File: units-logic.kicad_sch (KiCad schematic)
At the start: 19 parts, among them U29 74AUC2G04, U30 74AUC2G32, U31 74AUC2G32, U34 74AUC2G32, U35 74AUC2G32, U37 74AUC2G08, U38 74AUC2G32, U40 74AUC2G32, U6 74AUC2G04, U7 74AUC2G04, U8 74AUC2G04

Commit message: add : alimentation
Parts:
- removed unit 2 of U10
- removed unit 3 of U30
- removed unit 3 of U31
- removed unit 3 of U34
- removed unit 3 of U35
- removed unit 3 of U7
- added C22, C23, C24, C25, C26, C27, C28, C29, C30, C31, C32, C33, C34, C35, C36: 0.1u, symbol Device:C
- added U28: (no value), Package_TO_SOT_SMD:SOT-23-6, symbol CornetPrisme_Library:SN74LVC1G11
- added unit 3 of U29
- added U42, U46, U47, U48: 74AUC2G32, symbol 74xGxx:74AUC2G32
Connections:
- net +1V8: now reaches U9.14 (VCC)
- net +1V8: now also U11.5 (VCC), U36.14 (VCC), U37.8 (VCC), U38.8 (VCC), U39.14 (VCC), U40.8 (VCC), U41.14 (VCC), U8.5 (VCC), C22.2, C23.2, C24.2, C25.2, C26.2, C27.2, C28.2, C29.2, C30.2, C31.2, C32.2, C33.2, C34.2, C35.2, C36.2, U28.5 (VCC), U29.5 (VCC), U42.8 (VCC), U46.8 (VCC), U47.8 (VCC), U48.8 (VCC)
- net GND: now reaches U9.7 (GND)
- net GND: now also U11.2 (GND), U36.7 (GND), U37.4 (GND), U38.4 (GND), U39.7 (GND), U40.4 (GND), U41.7 (GND), U8.2 (GND), C22.1, C23.1, C24.1, C25.1, C26.1, C27.1, C28.1, C29.1, C30.1, C31.1, C32.1, C33.1, C34.1, C35.1, C36.1, U28.2 (GND), U29.2 (GND), U42.4 (GND), U46.4 (GND), U47.4 (GND), U48.4 (GND)
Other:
- moved on the sheet: U37C, U38C, U8C

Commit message: Branchement des pins
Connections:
- no-connect marks 0 -> 6

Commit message: ajout composants
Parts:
- removed C26: 0.1u, symbol Device:C
- removed U47: 74AUC2G32, symbol 74xGxx:74AUC2G32
- added C39: 0.1u, symbol Device:C
- added unit 2 of U10
- C22, C23, C24, C25, C27, C28, C29, C30, C31, C32, C33, C34, C35, C36: Basic (none) -> Y; JLCPCB Part # (none) -> C1591; Manufacturer (none) -> Samsung Electro-Mechanics; Manufacturer Part Number (none) -> CL10B104KB8NNNC
- U10, U11, U28, U32, U33: Basic (none) -> X; JLCPCB Part # (none) -> C22046; Manufacturer (none) -> TI; Manufacturer Part Number (none) -> SN74LVC1G11DBVR
- U30, U31, U34, U35, U38: Basic (none) -> X; JLCPCB Part # (none) -> C2876519; Manufacturer (none) -> TI; Manufacturer Part Number (none) -> SN74AUP2G32DCUR
- U30: renamed from U38; Basic (none) -> X; JLCPCB Part # (none) -> C2876519; Manufacturer (none) -> TI; Manufacturer Part Number (none) -> SN74AUP2G32DCUR
- U31: renamed from U40; Basic (none) -> X; JLCPCB Part # (none) -> C2876519; Manufacturer (none) -> TI; Manufacturer Part Number (none) -> SN74AUP2G32DCUR
- U34: renamed from U42; Basic (none) -> X; JLCPCB Part # (none) -> C2876519; Manufacturer (none) -> TI; Manufacturer Part Number (none) -> SN74AUP2G32DCUR
- U35: renamed from U46; Basic (none) -> X; JLCPCB Part # (none) -> C2876519; Manufacturer (none) -> TI; Manufacturer Part Number (none) -> SN74AUP2G32DCUR
- U36, U39, U41, U9: Basic (none) -> X; JLCPCB Part # (none) -> C2868761; Manufacturer (none) -> TI; Manufacturer Part Number (none) -> SN74ALVC08DR
- U37: Basic (none) -> X; JLCPCB Part # (none) -> C2860154; Manufacturer (none) -> TI; Manufacturer Part Number (none) -> SN74AUC2G08DCUR
- U38: renamed from U48; Basic (none) -> X; JLCPCB Part # (none) -> C2876519; Manufacturer (none) -> TI; Manufacturer Part Number (none) -> SN74AUP2G32DCUR
- U39: renamed from U41; Basic (none) -> X; JLCPCB Part # (none) -> C2868761; Manufacturer (none) -> TI; Manufacturer Part Number (none) -> SN74ALVC08DR
- U41: renamed from U39; Basic (none) -> X; JLCPCB Part # (none) -> C2868761; Manufacturer (none) -> TI; Manufacturer Part Number (none) -> SN74ALVC08DR
- U6: renamed from U29; Basic (none) -> X; JLCPCB Part # (none) -> C139318; Manufacturer (none) -> TI; Manufacturer Part Number (none) -> SN74AUP2G14DCKR
- U6, U7: Basic (none) -> X; JLCPCB Part # (none) -> C139318; Manufacturer (none) -> TI; Manufacturer Part Number (none) -> SN74AUP2G14DCKR
- U7: renamed from U8; Basic (none) -> X; JLCPCB Part # (none) -> C139318; Manufacturer (none) -> TI; Manufacturer Part Number (none) -> SN74AUP2G14DCKR
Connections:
- net +1V8: now also C39.2, U10.5 (VCC)
- net GND: now also C39.1, U10.2 (GND)

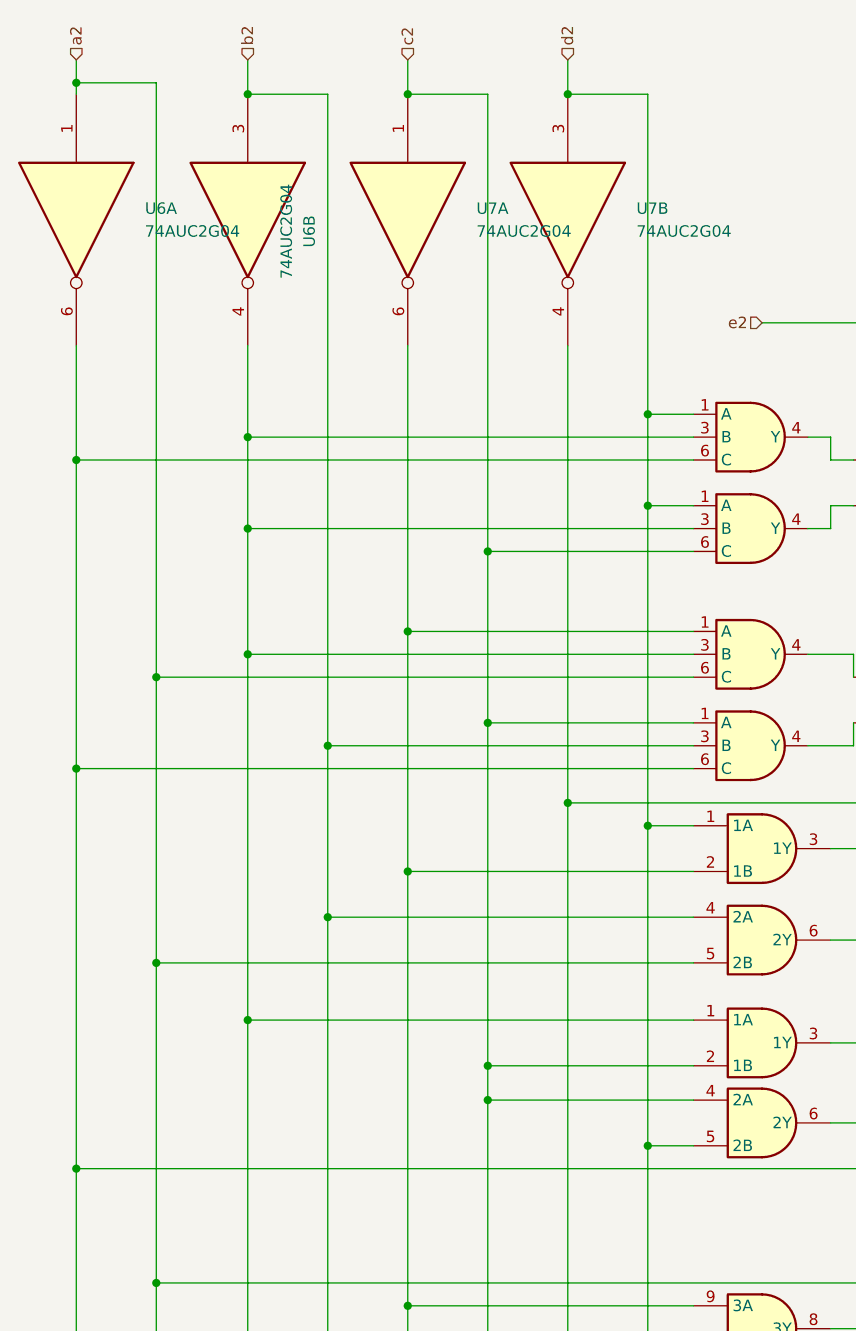
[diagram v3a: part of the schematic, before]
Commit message: elimination of errors
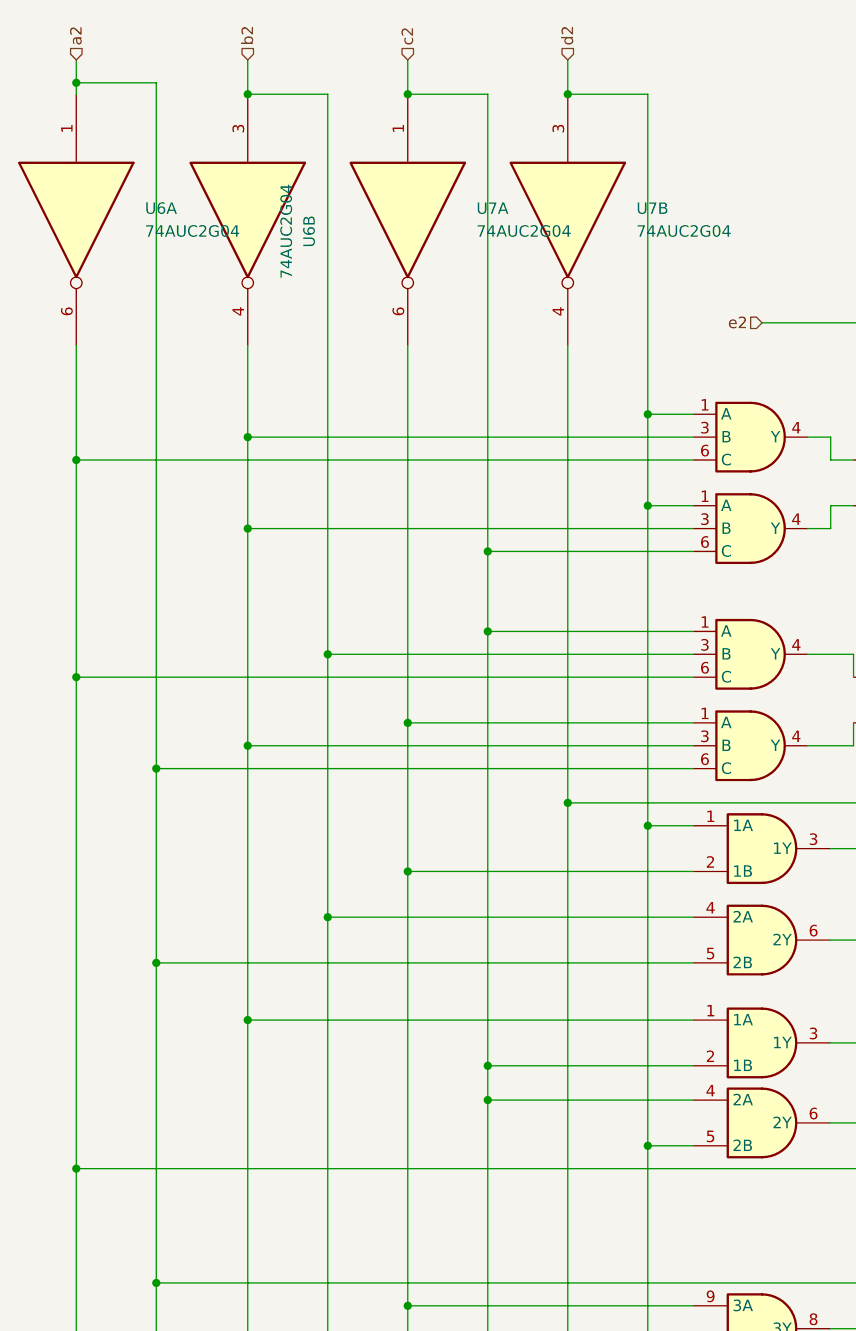
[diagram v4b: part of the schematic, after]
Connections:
- net a2: now also U33.6 (C); no longer U32.6 (C)
- net b2: now also U32.3 (B); no longer U33.3 (B)
- net c2: now also U32.1 (A); no longer U33.1 (A)
- net at U11.6 (C), U37.6, U39.5 (2B)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: now also U32.6 (C); no longer U33.6 (C)
- net at U36.13 (4B), U36.9 (3A), U39.4 (2A)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: now also U33.1 (A); no longer U32.1 (A)
- net at U10.3 (B), U11.3 (B), U36.1 (1A)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: now also U33.3 (B); no longer U32.3 (B)

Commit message: add footprint
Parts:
- added C50, C51: 0.1u, Capacitor_SMD:C_0603_1608Metric, symbol Device:C
- added unit 2 of U32
- added unit 2 of U33
- C22, C23, C24, C25, C27, C28, C29, C30, C31, C32, C33, C34, C35, C36, C39: footprint (none) -> Capacitor_SMD:C_0603_1608Metric
- U30, U31, U34, U35, U38: value 74AUC2G32 -> ²; footprint (none) -> Package_SO:VSSOP-8_3x3mm_P0.65mm
- U37: footprint (none) -> Package_SO:Texas_DGN0008B_VSSOP-8-1EP_3x3mm_P0.65mm_EP2x3mm_Mask1.88x1.98mm
- U6, U7: footprint (none) -> Package_TO_SOT_SMD:Texas_R-PDSO-G6
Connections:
- net +1V8: now also C50.2, C51.2, U32.5 (VCC), U33.5 (VCC)
- net GND: now also C50.1, C51.1, U32.2 (GND), U33.2 (GND)

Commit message: dbt positionnement
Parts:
- removed C31: 0.1u, Capacitor_SMD:C_0603_1608Metric, symbol Device:C
- removed U28: (no value), Package_TO_SOT_SMD:SOT-23-6, symbol CornetPrisme_Library:SN74LVC1G11
